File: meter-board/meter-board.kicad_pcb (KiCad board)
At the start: 2 copper layers, 0 parts

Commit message: modify pcb config
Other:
- copper layers 2 -> 4
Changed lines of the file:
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@@
 	(layers
 		(0 "F.Cu" signal)
+		(4 "In1.Cu" signal)
+		(6 "In2.Cu" signal)
 		(2 "B.Cu" signal)
 		(9 "F.Adhes" user "F.Adhesive")
@@
 		(43 "User.3" user)
 		(45 "User.4" user)
+		(47 "User.5" user)
+		(49 "User.6" user)
+		(51 "User.7" user)
+		(53 "User.8" user)
+		(55 "User.9" user)
 	)
 	(setup
@@
 			)
 			(layer "dielectric 1"
-				(type "core")
-				(thickness 0.71)
+				(type "prepreg")
+				(thickness 0.1)
 				(material "FR4")
 				(epsilon_r 4.5)
+				(loss_tangent 0.02)
+			)
+			(layer "In1.Cu"
+				(type "copper")
+				(thickness 0.035)
+			)
+			(layer "dielectric 2"
+				(type "core")
+				(thickness 0.44)
+				(material "FR4")
+				(epsilon_r 4.5)
+				(loss_tangent 0.02)
+			)
+			(layer "In2.Cu"
+				(type "copper")
+				(thickness 0.035)
+			)
+			(layer "dielectric 3"
+				(type "prepreg")
+				(thickness 0.1)
+				(material "FR4")
+				(epsilon_r 4.5)

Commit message: update layout
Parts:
- added C1: 4.7u, my_Capacitor:C_1206_3216M, B.Cu at (42.5, 44.5)
- added C10: UUD1H101MNL1GS, my_Capacitor:UUD1H101MNL1GS, B.Cu at (39.5, 37.0)
- added C11: 0.1u, my_Capacitor:C_0402_1005M, F.Cu at (4.00, 14.0)
- added C12: 0.1u, my_Capacitor:C_0402_1005M, F.Cu at (0.50, 19.5)
- added C13: 0.1u, my_Capacitor:C_0402_1005M, F.Cu at (0.50, 24.0)
- added C14: 0.1u, my_Capacitor:C_0402_1005M, F.Cu at (0.50, 28.5)
- added C15: 0.1u, my_Capacitor:C_0402_1005M, F.Cu at (33.5, 62.5)
- added C16: 0.1u, my_Capacitor:C_0402_1005M, F.Cu at (43.5, 62.5)
- added C17: 0.1u, my_Capacitor:C_0402_1005M, F.Cu at (57.0, 54.0)
- added C18: 0.1u, my_Capacitor:C_0402_1005M, F.Cu at (62.0, 54.0)
- added C19: 0.1u, ProjectEV_Capacitor:C_1005M, B.Cu at (94.5, 11.5)
- added C2: 4.7u, my_Capacitor:C_1206_3216M, B.Cu at (35.5, 45.5)
- added C20: 0.1u, ProjectEV_Capacitor:C_1005M, B.Cu at (94.5, 17.5)
- added C21: 0.1u, ProjectEV_Capacitor:C_1005M, F.Cu at (2.00, 34.5)
- added C22: 0.1u, ProjectEV_Capacitor:C_1005M, F.Cu at (113.2, 35.0)
- added C23: 1000p, my_Capacitor:C_1206_3216M, B.Cu at (12.5, 3.50)
- added C24: 10n, my_Capacitor:C_0402_1005M, F.Cu at (0.50, 26.5)
- added C25: 10n, my_Capacitor:C_0402_1005M, F.Cu at (0.50, 30.5)
- added C26: 10n, my_Capacitor:C_0402_1005M, F.Cu at (34.5, 69.0)
- added C27: 10n, my_Capacitor:C_0402_1005M, F.Cu at (45.5, 69.0)
- added C3: 10u, my_Capacitor:C_1206_3216M, F.Cu at (34.0, 45.5)
- added C4: 8p, my_Capacitor:C_0402_1005M, F.Cu at (27.5, 42.0)
- added C5: 0.1u, my_Capacitor:C_0402_1005M, F.Cu at (35.0, 43.5)
- added C6: 22u, my_Capacitor:C_1206_3216M, F.Cu at (35.0, 38.5)
- added C7: 22u, my_Capacitor:C_1206_3216M, F.Cu at (35.0, 36.0)
- added C8: 1u, my_Capacitor:C_0402_1005M, F.Cu at (31.0, 45.5)
- added C9: 6800p, my_Capacitor:C_0402_1005M, F.Cu at (27.5, 40.0)
- added D1: DF2B36FU,H3F, my_Protection:DF2B36FU,H3F, B.Cu at (52.5, 39.5)
- added D10: XZM2CRK45WT-9, my_LED:XZM2CRK45WT-9, B.Cu at (16.5, 30.5)
- added D11: XZM2CRK45WT-9, my_LED:XZM2CRK45WT-9, B.Cu at (16.5, 35.5)
- added D12: XZM2CRK45WT-9, my_LED:XZM2CRK45WT-9, B.Cu at (16.5, 40.5)
- added D13: XZM2CRK45WT-9, my_LED:XZM2CRK45WT-9, B.Cu at (16.5, 45.5)
- added D14: XZM2CRK45WT-9, my_LED:XZM2CRK45WT-9, B.Cu at (22.5, 40.5)
- added D15: XZM2CRK45WT-9, my_LED:XZM2CRK45WT-9, B.Cu at (27.5, 33.0)
- added D16: XZM2CRK45WT-9, my_LED:XZM2CRK45WT-9, B.Cu at (32.5, 28.0)
- added D17: XZM2CRK45WT-9, my_LED:XZM2CRK45WT-9, B.Cu at (37.5, 23.0)
- added D18: XZM2CRK45WT-9, my_LED:XZM2CRK45WT-9, B.Cu at (42.5, 20.5)
- added D19: XZM2CRK45WT-9, my_LED:XZM2CRK45WT-9, B.Cu at (47.5, 18.0)
- added D2: MM3Z12VST1G, my_Diode:MM3Z12VST1G, B.Cu at (45.5, 43.0)
- added D20: XZM2CRK45WT-9, my_LED:XZM2CRK45WT-9, B.Cu at (52.5, 18.0)
- added D21: XZM2CRK45WT-9, my_LED:XZM2CRK45WT-9, B.Cu at (57.5, 18.0)
- added D22: XZM2CRK45WT-9, my_LED:XZM2CRK45WT-9, B.Cu at (62.5, 18.0)
- added D23: XZM2CRK45WT-9, my_LED:XZM2CRK45WT-9, B.Cu at (67.5, 18.0)
- added D24: XZM2DG45WT-9, my_LED:XZM2DG45WT-9, B.Cu at (85.0, 25.5)
- added D25: XZM2DG45WT-9, my_LED:XZM2DG45WT-9, B.Cu at (85.0, 30.5)
- added D26: XZM2DG45WT-9, my_LED:XZM2DG45WT-9, B.Cu at (85.0, 35.5)
- added D27: XZM2DG45WT-9, my_LED:XZM2DG45WT-9, B.Cu at (85.0, 40.5)
- added D28: XZM2DG45WT-9, my_LED:XZM2DG45WT-9, B.Cu at (85.0, 45.5)
- added D29: XZM2DG45WT-9, my_LED:XZM2DG45WT-9, B.Cu at (17.5, 6.50)
- added D3: LTW-E670DS, my_LED:LTW-E670DS, F.Cu at (12.5, 13.0)
- added D30: XZM2DG45WT-9, my_LED:XZM2DG45WT-9, B.Cu at (22.5, 6.50)
- added D31: XZM2DG45WT-9, my_LED:XZM2DG45WT-9, B.Cu at (27.5, 6.50)
- added D32: XZM2DG45WT-9, my_LED:XZM2DG45WT-9, B.Cu at (32.5, 6.50)
- added D33: XZM2DG45WT-9, my_LED:XZM2DG45WT-9, B.Cu at (37.5, 6.50)
- added D34: XZM2DG45WT-9, my_LED:XZM2DG45WT-9, B.Cu at (42.5, 6.50)
- added D35: XZM2CRK45WT-9, my_LED:XZM2CRK45WT-9, B.Cu at (47.5, 6.50)
- added D36: XZM2CRK45WT-9, my_LED:XZM2CRK45WT-9, B.Cu at (52.5, 6.50)
- added D37: XZM2CRK45WT-9, my_LED:XZM2CRK45WT-9, B.Cu at (57.5, 6.50)
- added D38: XZM2CRK45WT-9, my_LED:XZM2CRK45WT-9, B.Cu at (62.5, 6.50)
- added D39: XZM2CRK45WT-9, my_LED:XZM2CRK45WT-9, B.Cu at (67.5, 6.50)
- added D4: LTW-E670DS, my_LED:LTW-E670DS, F.Cu at (17.5, 13.0)
- added D40: XZM2CRK45WT-9, my_LED:XZM2CRK45WT-9, B.Cu at (72.5, 6.50)
- added D41: BAS70-04-E3-08, my_Diode:BAS70-04-E3-08, B.Cu at (31.0, 99.0)
- added D42: BAS70-04-E3-08, my_Diode:BAS70-04-E3-08, B.Cu at (31.0, 103.5)
- added D43: BAS70-04-E3-08, my_Diode:BAS70-04-E3-08, B.Cu at (29.9, 87.5)
- added D44: BAS70-04-E3-08, my_Diode:BAS70-04-E3-08, B.Cu at (33.5, 87.5)
- added D45: BAS70-04-E3-08, my_Diode:BAS70-04-E3-08, B.Cu at (26.4, 99.0)
- added D46: BAS70-04-E3-08, my_Diode:BAS70-04-E3-08, B.Cu at (26.4, 103.5)
- added D47: BAS70-04-E3-08, my_Diode:BAS70-04-E3-08, B.Cu at (26.4, 107.9)
- added D48: DF2B36FU,H3F, my_Protection:DF2B36FU,H3F, B.Cu at (70.5, 104.0)
- added D49: DF2B36FU,H3F, my_Protection:DF2B36FU,H3F, B.Cu at (40.0, 92.5)
- added D5: LTW-E670DS, my_LED:LTW-E670DS, F.Cu at (22.5, 13.0)
- added D50: DF2B36FU,H3F, my_Protection:DF2B36FU,H3F, B.Cu at (29.9, 94.5)
- added D51: DF2B36FU,H3F, my_Protection:DF2B36FU,H3F, B.Cu at (45.0, 100.0)
- added D52: DF2B36FU,H3F, my_Protection:DF2B36FU,H3F, B.Cu at (40.0, 104.5)
- added D53: DF2B36FU,H3F, my_Protection:DF2B36FU,H3F, B.Cu at (40.5, 109.0)
- added D54: DF2B36FU,H3F, my_Protection:DF2B36FU,H3F, B.Cu at (53.0, 99.5)
- added D55: 150060GS75003, my_LED:150060GS75003, F.Cu at (26.5, 44.0)
- added D6: LTW-E670DS, my_LED:LTW-E670DS, F.Cu at (27.5, 13.0)
- added D7: XZM2CRK45WT, my_LED:XZM2CRK45WT, F.Cu at (80.0, 6.50)
- added D8: XZMECBDDG45SHTA, my_LED:XZMECBDDG45SHTA, F.Cu at (32.5, 13.0)
- added D9: XZM2CRK45WT-9, my_LED:XZM2CRK45WT-9, B.Cu at (16.5, 25.5)
- added F1: 0686F0500-01, my_Fuse:0686F0500-01, B.Cu at (49.5, 40.0)
- added FB1: MMZ1005Y102CT000, my_Filter:MMZ1005Y102CT000, B.Cu at (42.0, 31.5)
- added FL1: ACP3225-102-2P-T000, my_Filter:ACP3225-102-2P-T000, B.Cu at (39.0, 44.5)
- added H1: MountingHole_4.3mm_M4_Pad_Via, my_Mechanical:MountingHole_4.3mm_M4_Pad_Via, F.Cu at (5.00, 5.00)
- added H2: MountingHole_4.3mm_M4_Pad_Via, my_Mechanical:MountingHole_4.3mm_M4_Pad_Via, F.Cu at (5.00, 45.0)
- added H3: MountingHole_4.3mm_M4_Pad_Via, my_Mechanical:MountingHole_4.3mm_M4_Pad_Via, F.Cu at (95.0, 45.0)
- added H4: MountingHole_4.3mm_M4_Pad_Via, my_Mechanical:MountingHole_4.3mm_M4_Pad_Via, F.Cu at (95.0, 5.00)
- added J1: 2-1445053-2, my_Connector:2-1445053-2, B.Cu at (51.0, 46.5)
- added J2: 3-794636-8, my_Connector:3-794636-8, B.Cu at (68.5, 34.0)
- added J3: 2-1445053-4, my_Connector:2-1445053-4, B.Cu at (68.5, 46.5)
- added JP1: SolderJumper-2_P1.3mm_Open_RoundedPad1.0x1.5mm, my_Jumper:SolderJumper-2_P1.3mm_Open_RoundedPad1.0x1.5mm, F.Cu at (24.5, 46.5)
- added JP2: SolderJumper-2_P1.3mm_Open_RoundedPad1.0x1.5mm, my_Jumper:SolderJumper-2_P1.3mm_Open_RoundedPad1.0x1.5mm, F.Cu at (27.0, 46.5)
- added L1: SRP2512TMA-2R2M, my_Inductor:SRP2512TMA-2R2M, F.Cu at (36.5, 41.5)
- added Q1: PMN100EPAX, my_Transistor:PMN100EPAX, B.Cu at (46.5, 40.0)
- added Q2: 2N7002K-AU_R1_000A2, my_Transistor:2N7002K-AU_R1_000A2, B.Cu at (26.0, 46.0)
- added R1: 10k, my_Resistor:R_0402_1005M, B.Cu at (48.0, 43.0)
- added R10: 2.2k, my_Resistor:R_0402_1005M, B.Cu at (20.0, 3.50)
- added R100: 100k, my_Resistor:R_0402_1005M, F.Cu at (94.0, 28.0)
- added R101: 100k, my_Resistor:R_0402_1005M, F.Cu at (94.0, 29.0)
- added R102: 100k, my_Resistor:R_0402_1005M, F.Cu at (94.0, 30.0)
- added R103: 100k, my_Resistor:R_0402_1005M, F.Cu at (94.0, 31.0)
- added R104: 100k, my_Resistor:R_0402_1005M, F.Cu at (94.0, 32.0)
- added R105: 100k, my_Resistor:R_0402_1005M, F.Cu at (94.0, 33.0)
- added R106: 100k, my_Resistor:R_0402_1005M, B.Cu at (24.5, 18.0)
- added R107: 100k, my_Resistor:R_0402_1005M, B.Cu at (24.5, 19.0)
- added R108: 100k, my_Resistor:R_0402_1005M, B.Cu at (24.5, 20.0)
- added R109: 100k, my_Resistor:R_0402_1005M, B.Cu at (24.5, 21.0)
- added R11: 2.2k, my_Resistor:R_0402_1005M, B.Cu at (25.0, 3.50)
- added R110: 100k, my_Resistor:R_0402_1005M, B.Cu at (24.5, 22.0)
- added R111: 100k, my_Resistor:R_0402_1005M, B.Cu at (24.5, 23.0)
- added R112: 100k, my_Resistor:R_0402_1005M, B.Cu at (24.5, 24.0)
- added R113: 100k, my_Resistor:R_0402_1005M, B.Cu at (24.5, 25.0)
- added R114: ST-4ETA103, my_Resistor:ST-4ETA103, B.Cu at (20.0, 65.0)
- added R115: ST-4ETA103, my_Resistor:ST-4ETA103, B.Cu at (27.0, 65.0)
- added R116: ST-4ETA103, my_Resistor:ST-4ETA103, B.Cu at (56.0, 63.5)
- added R117: ST-4ETA103, my_Resistor:ST-4ETA103, B.Cu at (62.0, 63.5)
- added R118: 220, my_Resistor:R_0603_1608M, B.Cu at (77.5, 5.00)
- added R119: 220, my_Resistor:R_0603_1608M, B.Cu at (77.5, 6.50)
- added R12: 2.2k, my_Resistor:R_0402_1005M, B.Cu at (30.0, 3.50)
- added R120: 220, my_Resistor:R_0603_1608M, B.Cu at (77.5, 8.00)
- added R121: 220, my_Resistor:R_0603_1608M, B.Cu at (77.5, 9.50)
- added R122: 220, my_Resistor:R_0603_1608M, B.Cu at (77.5, 11.0)
- added R123: 220, my_Resistor:R_0603_1608M, B.Cu at (77.5, 12.5)
- added R124: 220, my_Resistor:R_0603_1608M, B.Cu at (77.5, 14.0)
- added R125: 220, my_Resistor:R_0603_1608M, B.Cu at (77.5, 15.5)
- added R126: 100k, my_Resistor:R_0402_1005M, B.Cu at (89.0, 7.00)
- added R127: 100k, my_Resistor:R_0402_1005M, B.Cu at (89.0, 8.00)
- added R128: 100k, my_Resistor:R_0402_1005M, B.Cu at (89.0, 9.00)
- added R129: 100k, my_Resistor:R_0402_1005M, B.Cu at (89.0, 10.0)
- added R13: 2.2k, my_Resistor:R_0402_1005M, B.Cu at (35.0, 3.50)
- added R130: 100k, my_Resistor:R_0402_1005M, B.Cu at (89.0, 11.0)
- added R131: 100k, my_Resistor:R_0402_1005M, B.Cu at (89.0, 12.0)
- added R132: 100k, my_Resistor:R_0402_1005M, B.Cu at (89.0, 13.0)
- added R133: 100k, my_Resistor:R_0402_1005M, B.Cu at (89.0, 14.0)
- added R134: 100k, my_Resistor:R_0402_1005M, B.Cu at (89.0, 15.0)
- added R135: 100k, my_Resistor:R_0402_1005M, B.Cu at (89.0, 16.0)
- added R136: 100k, my_Resistor:R_0402_1005M, B.Cu at (89.0, 17.0)
- added R137: 100k, my_Resistor:R_0402_1005M, B.Cu at (89.0, 18.0)
- added R138: 100k, my_Resistor:R_0402_1005M, B.Cu at (89.0, 19.0)
- added R139: 100k, my_Resistor:R_0402_1005M, B.Cu at (89.0, 20.0)
- added R14: 2.2k, my_Resistor:R_0402_1005M, B.Cu at (40.0, 3.50)
- added R140: 100k, my_Resistor:R_0402_1005M, B.Cu at (89.0, 21.0)
- added R141: 100k, my_Resistor:R_0402_1005M, B.Cu at (89.0, 22.0)
- added R142: 100k, my_Resistor:R_0402_1005M, B.Cu at (10.5, 33.0)
- added R143: 100k, my_Resistor:R_0402_1005M, B.Cu at (10.5, 34.0)
- added R144: 100k, my_Resistor:R_0402_1005M, B.Cu at (10.5, 35.0)
- added R145: 100k, my_Resistor:R_0402_1005M, B.Cu at (10.5, 36.0)
- added R146: 100k, my_Resistor:R_0402_1005M, B.Cu at (10.5, 37.0)
- added R147: 100k, my_Resistor:R_0402_1005M, B.Cu at (10.5, 38.0)
- added R148: 100k, my_Resistor:R_0402_1005M, B.Cu at (10.5, 39.0)
- added R149: 100k, my_Resistor:R_0402_1005M, B.Cu at (10.5, 40.0)
- added R15: 2.2k, my_Resistor:R_0402_1005M, B.Cu at (45.0, 3.50)
- added R150: 100k, my_Resistor:R_0402_1005M, F.Cu at (111.2, 28.1)
- added R151: 100k, my_Resistor:R_0402_1005M, F.Cu at (111.2, 30.1)
- added R152: 100k, my_Resistor:R_0402_1005M, F.Cu at (111.2, 32.0)
- added R153: 100k, my_Resistor:R_0402_1005M, F.Cu at (-1.50, 26.5)
- added R154: 100k, my_Resistor:R_0402_1005M, F.Cu at (0.50, 31.5)
- added R155: 100k, my_Resistor:R_0402_1005M, F.Cu at (34.5, 68.0)
- added R156: 100k, my_Resistor:R_0402_1005M, F.Cu at (45.5, 68.0)
- added R157: 100, my_Resistor:R_0402_1005M, B.Cu at (23.9, 91.5)
- added R158: 100, my_Resistor:R_0402_1005M, B.Cu at (39.0, 113.5)
- added R159: 100, my_Resistor:R_0402_1005M, B.Cu at (29.9, 91.5)
- added R16: 2.2k, my_Resistor:R_0402_1005M, B.Cu at (50.0, 3.50)
- added R160: 100, my_Resistor:R_0402_1005M, B.Cu at (36.0, 97.9)
- added R161: 100, my_Resistor:R_0402_1005M, B.Cu at (36.0, 99.8)
- added R162: 100, my_Resistor:R_0402_1005M, B.Cu at (36.0, 101.8)
- added R163: 100, my_Resistor:R_0402_1005M, B.Cu at (36.0, 103.8)
- added R164: 1M, my_Resistor:R_1206_3216M, B.Cu at (12.5, 6.50)
- added R165: 100k, my_Resistor:R_0402_1005M, F.Cu at (24.5, 44.0)
- added R166: 100k, my_Resistor:R_0402_1005M, B.Cu at (28.5, 45.0)
- added R167: 100, my_Resistor:R_0402_1005M, B.Cu at (28.5, 43.0)
- added R17: 2.2k, my_Resistor:R_0402_1005M, B.Cu at (55.0, 3.50)
- added R18: 2.2k, my_Resistor:R_0402_1005M, B.Cu at (60.0, 3.50)
- added R19: 2.2k, my_Resistor:R_0402_1005M, B.Cu at (65.0, 3.50)
- added R2: 100k, my_Resistor:R_0402_1005M, F.Cu at (30.0, 37.0)
- added R20: 2.2k, my_Resistor:R_0402_1005M, B.Cu at (70.0, 3.50)
- added R21: 2.2k, my_Resistor:R_0402_1005M, B.Cu at (75.0, 3.50)
- added R22: 2.2k, my_Resistor:R_0402_1005M, F.Cu at (15.0, 15.0)
- added R23: 2.2k, my_Resistor:R_0402_1005M, F.Cu at (20.0, 15.0)
- added R24: 2.2k, my_Resistor:R_0402_1005M, F.Cu at (25.0, 15.0)
- added R25: 2.2k, my_Resistor:R_0402_1005M, F.Cu at (30.0, 15.0)
- added R26: 2.2k, my_Resistor:R_0402_1005M, F.Cu at (34.5, 17.0)
- added R27: 2.2k, my_Resistor:R_0402_1005M, F.Cu at (32.5, 17.0)
- added R28: 2.2k, my_Resistor:R_0402_1005M, F.Cu at (33.5, 17.0)
- added R29: 2.2k, my_Resistor:R_0402_1005M, B.Cu at (13.5, 23.0)
- added R3: 18k, my_Resistor:R_0402_1005M, F.Cu at (30.0, 38.0)
- added R30: 2.2k, my_Resistor:R_0402_1005M, B.Cu at (13.5, 28.0)
- added R31: 2.2k, my_Resistor:R_0402_1005M, B.Cu at (13.5, 33.0)
- added R32: 2.2k, my_Resistor:R_0402_1005M, B.Cu at (13.5, 38.0)
- added R33: 2.2k, my_Resistor:R_0402_1005M, B.Cu at (13.5, 43.0)
- added R34: 2.2k, my_Resistor:R_0402_1005M, B.Cu at (22.5, 35.5)
- added R35: 2.2k, my_Resistor:R_0402_1005M, B.Cu at (27.5, 28.0)
- added R36: 2.2k, my_Resistor:R_0402_1005M, B.Cu at (32.5, 23.0)
- added R37: 2.2k, my_Resistor:R_0402_1005M, B.Cu at (37.5, 18.0)
- added R38: 2.2k, my_Resistor:R_0402_1005M, B.Cu at (42.5, 15.5)
- added R39: 2.2k, my_Resistor:R_0402_1005M, B.Cu at (47.5, 13.0)
- added R4: 100k, my_Resistor:R_0402_1005M, F.Cu at (26.5, 42.0)
- added R40: 2.2k, my_Resistor:R_0402_1005M, B.Cu at (52.5, 13.0)
- added R41: 2.2k, my_Resistor:R_0402_1005M, B.Cu at (57.5, 13.0)
- added R42: 2.2k, my_Resistor:R_0402_1005M, B.Cu at (62.5, 13.0)
- added R43: 2.2k, my_Resistor:R_0402_1005M, B.Cu at (67.5, 13.0)
- added R44: 2.2k, my_Resistor:R_0402_1005M, F.Cu at (78.5, 4.00)
- added R45: 2.2k, my_Resistor:R_0402_1005M, B.Cu at (82.0, 23.0)
- added R46: 2.2k, my_Resistor:R_0402_1005M, B.Cu at (82.0, 28.0)
- added R47: 2.2k, my_Resistor:R_0402_1005M, B.Cu at (82.0, 33.0)
- added R48: 2.2k, my_Resistor:R_0402_1005M, B.Cu at (82.0, 38.0)
- added R49: 2.2k, my_Resistor:R_0402_1005M, B.Cu at (82.0, 43.0)
- added R5: 19.1k, my_Resistor:R_0402_1005M, F.Cu at (28.5, 43.0)
- added R50: 2.2k, my_Resistor:R_0402_1005M, B.Cu at (7.50, 15.0)
- added R51: 2.2k, my_Resistor:R_0402_1005M, B.Cu at (7.50, 16.0)
- added R52: 2.2k, my_Resistor:R_0402_1005M, B.Cu at (7.50, 17.0)
- added R53: 2.2k, my_Resistor:R_0402_1005M, B.Cu at (7.50, 18.0)
- added R54: 2.2k, my_Resistor:R_0402_1005M, B.Cu at (7.50, 19.0)
- added R55: 2.2k, my_Resistor:R_0402_1005M, B.Cu at (7.50, 20.0)
- added R56: 2.2k, my_Resistor:R_0402_1005M, B.Cu at (7.50, 21.0)
- added R57: 2.2k, my_Resistor:R_0402_1005M, B.Cu at (7.50, 22.0)
- added R58: 2.2k, my_Resistor:R_0402_1005M, B.Cu at (7.50, 23.0)
- added R59: 2.2k, my_Resistor:R_0402_1005M, B.Cu at (7.50, 24.0)
- added R6: 82k, my_Resistor:R_0402_1005M, F.Cu at (30.0, 39.0)
- added R60: 2.2k, my_Resistor:R_0402_1005M, B.Cu at (7.50, 25.0)
- added R61: 2.2k, my_Resistor:R_0402_1005M, B.Cu at (7.50, 26.0)
- added R62: 2.2k, my_Resistor:R_0402_1005M, B.Cu at (7.50, 27.0)
- added R63: 2.2k, my_Resistor:R_0402_1005M, F.Cu at (16.0, 65.0)
- added R64: 2.2k, my_Resistor:R_0402_1005M, F.Cu at (16.0, 66.0)
- added R65: 2.2k, my_Resistor:R_0402_1005M, F.Cu at (16.0, 67.0)
- added R66: 2.2k, my_Resistor:R_0402_1005M, F.Cu at (16.0, 68.0)
- added R67: 2.2k, my_Resistor:R_0402_1005M, F.Cu at (38.0, 62.0)
- added R68: 2.2k, my_Resistor:R_0402_1005M, F.Cu at (38.0, 63.0)
- added R69: 2.2k, my_Resistor:R_0402_1005M, F.Cu at (38.0, 64.0)
- added R7: 9.1k, my_Resistor:R_0402_1005M, B.Cu at (32.0, 39.0)
- added R70: 2.2k, my_Resistor:R_0402_1005M, F.Cu at (38.0, 65.0)
- added R71: 2.2k, my_Resistor:R_0402_1005M, F.Cu at (38.0, 66.0)
- added R72: 2.2k, my_Resistor:R_0402_1005M, F.Cu at (38.0, 67.0)
- added R73: 1k, my_Resistor:R_0402_1005M, F.Cu at (52.0, 65.0)
- added R74: 1k, my_Resistor:R_0402_1005M, F.Cu at (52.0, 57.0)
- added R75: 1k, my_Resistor:R_0402_1005M, F.Cu at (52.0, 58.0)
- added R76: 1k, my_Resistor:R_0402_1005M, F.Cu at (52.0, 59.0)
- added R77: 1k, my_Resistor:R_0402_1005M, F.Cu at (52.0, 60.0)
- added R78: 1k, my_Resistor:R_0402_1005M, F.Cu at (52.0, 61.0)
- added R79: 1k, my_Resistor:R_0402_1005M, F.Cu at (52.0, 62.0)
- added R8: 3k, my_Resistor:R_0402_1005M, B.Cu at (30.0, 39.0)
- added R80: 1k, my_Resistor:R_0402_1005M, F.Cu at (52.0, 63.0)
- added R81: 1k, my_Resistor:R_0402_1005M, F.Cu at (52.0, 64.0)
- added R82: 100k, my_Resistor:R_0402_1005M, B.Cu at (10.5, 15.0)
- added R83: 100k, my_Resistor:R_0402_1005M, B.Cu at (10.5, 16.0)
- added R84: 100k, my_Resistor:R_0402_1005M, B.Cu at (10.5, 17.0)
- added R85: 100k, my_Resistor:R_0402_1005M, B.Cu at (10.5, 18.0)
- added R86: 100k, my_Resistor:R_0402_1005M, B.Cu at (10.5, 19.0)
- added R87: 100k, my_Resistor:R_0402_1005M, B.Cu at (10.5, 20.0)
- added R88: 100k, my_Resistor:R_0402_1005M, B.Cu at (10.5, 21.0)
- added R89: 100k, my_Resistor:R_0402_1005M, B.Cu at (10.5, 22.0)
- added R9: 1k, my_Resistor:R_1206_3216M, B.Cu at (34.0, 40.5)
- added R90: 100k, my_Resistor:R_0402_1005M, B.Cu at (10.5, 24.0)
- added R91: 100k, my_Resistor:R_0402_1005M, B.Cu at (10.5, 25.0)
- added R92: 100k, my_Resistor:R_0402_1005M, B.Cu at (10.5, 26.0)
- added R93: 100k, my_Resistor:R_0402_1005M, B.Cu at (10.5, 27.0)
- added R94: 100k, my_Resistor:R_0402_1005M, B.Cu at (10.5, 28.0)
- added R95: 100k, my_Resistor:R_0402_1005M, B.Cu at (10.5, 29.0)
- added R96: 100k, my_Resistor:R_0402_1005M, B.Cu at (10.5, 30.0)
- added R97: 100k, my_Resistor:R_0402_1005M, B.Cu at (10.5, 31.0)
- added R98: 100k, my_Resistor:R_0402_1005M, F.Cu at (94.0, 26.0)
- added R99: 100k, my_Resistor:R_0402_1005M, F.Cu at (94.0, 27.0)
- added U1: AP66300QFVBW-13, my_Regulator:AP66300QFVBW-13, F.Cu at (31.5, 42.0)
- added U10: TLV1814RTER, my_Comparator:TLV1814RTER, F.Cu at (3.50, 21.0)
- added U11: TLV1814RTER, my_Comparator:TLV1814RTER, F.Cu at (3.50, 25.5)
- added U12: TLV1814RTER, my_Comparator:TLV1814RTER, F.Cu at (3.50, 30.0)
- added U13: TLV1814RTER, my_Comparator:TLV1814RTER, F.Cu at (34.0, 65.0)
- added U14: TLV1814RTER, my_Comparator:TLV1814RTER, F.Cu at (44.5, 65.0)
- added U15: TLV1814RTER, my_Comparator:TLV1814RTER, F.Cu at (57.5, 56.5)
- added U16: TBD62183AFNG,EL, my_PMIC:TBD62183AFNG,EL, F.Cu at (10.0, 19.0)
- added U17: TBD62183AFNG,EL, my_PMIC:TBD62183AFNG,EL, F.Cu at (10.0, 28.0)
- added U18: TBD62183AFNG,EL, my_PMIC:TBD62183AFNG,EL, B.Cu at (94.0, 30.0)
- added U19: TBD62183AFNG,EL, my_PMIC:TBD62183AFNG,EL, F.Cu at (24.5, 22.0)
- added U2: TS431BIYLT, my_Reference:TS431BIYLT, B.Cu at (32.5, 36.5)
- added U20: TLV1814RTER, my_Comparator:TLV1814RTER, F.Cu at (63.0, 56.5)
- added U21: SN74HC595BRWNR, my_Logic:SN74HC595BRWNR, B.Cu at (94.5, 14.0)
- added U22: SN74HC595BRWNR, my_Logic:SN74HC595BRWNR, B.Cu at (94.5, 20.0)
- added U23: SN74HC595BRWNR, my_Logic:SN74HC595BRWNR, F.Cu at (3.50, 37.0)
- added U24: TBD62783AFNG,EL, my_PMIC:TBD62783AFNG,EL, B.Cu at (83.5, 11.0)
- added U25: TBD62183AFNG,EL, my_PMIC:TBD62183AFNG,EL, B.Cu at (83.5, 19.0)
- added U26: TBD62183AFNG,EL, my_PMIC:TBD62183AFNG,EL, F.Cu at (10.0, 37.0)
- added U27: SN74LV4T125RGYR, my_Logic:SN74LV4T125RGYR, F.Cu at (111.3, 38.0)
- added U3: ACSC02-41SURKWA-F01, my_LED:ACSC02-41SURKWA-F01, F.Cu at (75.0, 16.5)
- added U4: ACSC02-41SURKWA-F01, my_LED:ACSC02-41SURKWA-F01, F.Cu at (82.5, 16.5)
- added U5: ACSC02-41SURKWA-F01, my_LED:ACSC02-41SURKWA-F01, F.Cu at (90.0, 16.5)
- added U6: 157121S12700, my_LED:157121S12700, F.Cu at (44.0, 38.5)
- added U7: 157121S12700, my_LED:157121S12700, F.Cu at (54.5, 38.5)
- added U8: 157121S12700, my_LED:157121S12700, F.Cu at (65.0, 38.5)
- added U9: TLV1814RTER, my_Comparator:TLV1814RTER, F.Cu at (3.50, 16.5)
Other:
- board outline added: 100 x 50 mm
- board text added: "V"
- board text added: "km/h"

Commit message: update layout
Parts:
- C19, C20, U18, U21, U22: moved to F.Cu
- C24, R100, R101, R102, R103, R104, R105, R153, R63, R64, R65, R66, R98, R99: moved to B.Cu
- moved D47 84.9 mm to (78.0, 40.5), turned to -90 degrees
- moved R158 77.7 mm to (64.0, 40.0)
- moved D46 77.6 mm to (74.5, 42.5), turned to -90 degrees
- moved D53 77.3 mm to (74.5, 39.5), turned to 0 degrees
- moved D45 73.6 mm to (78.0, 46.5), turned to -90 degrees
- moved D52 71.9 mm to (78.0, 43.5), turned to 0 degrees
- moved R163 71.4 mm to (71.0, 41.5), turned to 0 degrees
- moved R162 68.2 mm to (68.0, 41.5), turned to 0 degrees
- moved D51 67.6 mm to (54.0, 33.0)
- moved R160 67.1 mm to (70.0, 40.0)
- moved D54 66.8 mm to (78.0, 37.5), turned to 0 degrees
- moved D42 65.6 mm to (54.0, 42.0), turned to 90 degrees
- moved D50 65.5 mm to (57.5, 35.0), turned to 180 degrees
- moved R161 65.1 mm to (65.0, 41.5), turned to 0 degrees
- moved D48 64.3 mm to (57.5, 41.0), turned to 180 degrees
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
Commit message: layout of components is finished
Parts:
- moved D14 0.50 mm to (22.5, 41.0)
- moved Q2 0.50 mm to (26.5, 46.0)
- moved R166 0.50 mm to (29.0, 45.0)
- moved R167 0.50 mm to (29.0, 43.0)

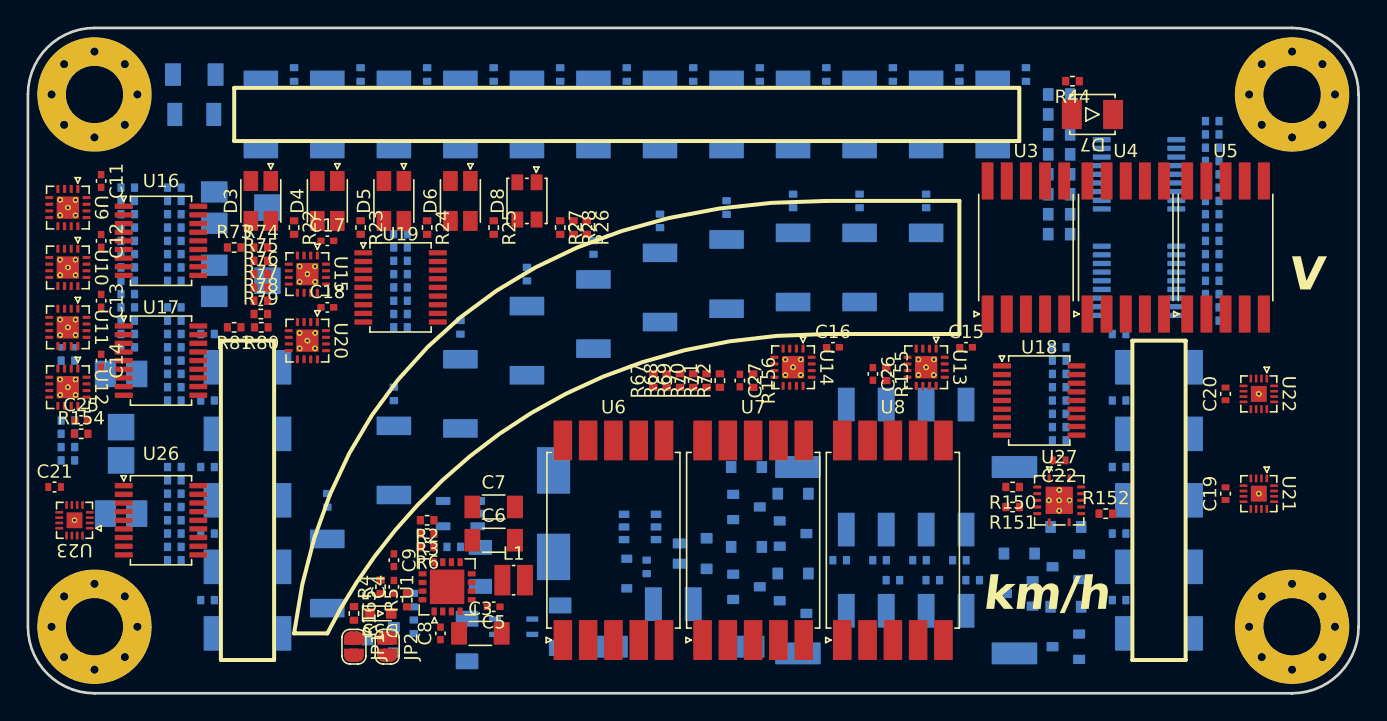
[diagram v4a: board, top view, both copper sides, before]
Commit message: update wiring
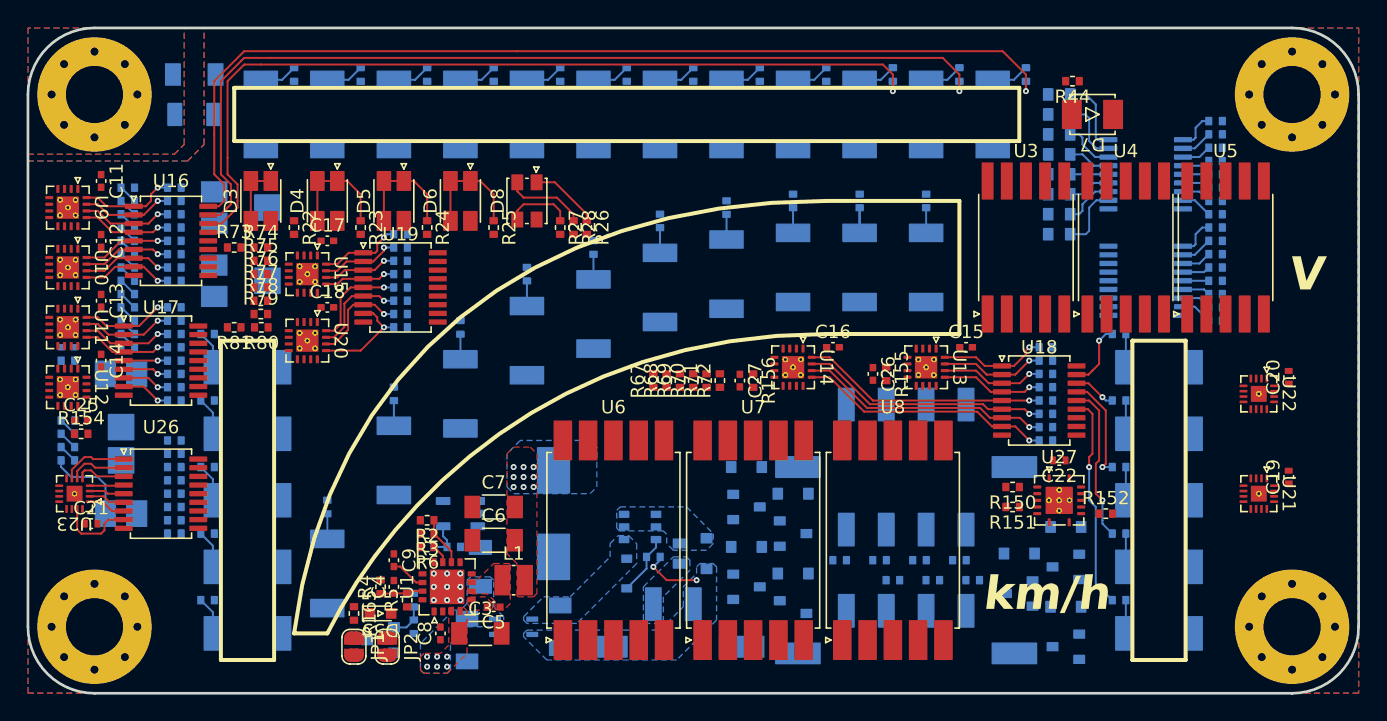
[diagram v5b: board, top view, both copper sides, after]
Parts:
- moved C19 4.91 mm to (94.8, 33.8)
- moved C20 4.91 mm to (94.8, 26.2)
- moved C21 3.89 mm to (4.75, 37.2)
- moved R142 2.00 mm to (11.0, 31.0)
- moved R143 2.00 mm to (11.0, 32.0)
- moved R144 2.00 mm to (11.0, 33.0)
- moved R145 2.00 mm to (11.0, 34.0)
- moved R146 2.00 mm to (11.0, 35.0)
- moved R147 2.00 mm to (11.0, 36.0)
- moved R148 2.00 mm to (11.0, 37.0)
- moved R149 2.00 mm to (11.0, 38.0)
- moved U23 2.00 mm to (3.50, 35.0)
- moved U26 2.00 mm to (10.0, 35.0)
- moved R100 1.00 mm to (76.5, 26.0)
- moved R101 1.00 mm to (76.5, 27.0)
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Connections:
- D8 pad 2: (no net) -> +5VD
- J1 pad MP1: GND -> Net-(D1-A2)
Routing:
- net /G6R6_R6: track 0.00 -> 75.3 mm, vias 0 -> 1
- net /G6R6_R5: track 0.00 -> 70.3 mm, vias 0 -> 1
- net /G6R6_R4: track 0.00 -> 65.3 mm, vias 0 -> 1
- net Net-(U18-I8): track 0.00 -> 19.1 mm, vias 0 -> 1
- net Net-(U18-I7): track 0.00 -> 18.9 mm, vias 0 -> 1
- net Net-(U18-I6): track 0.00 -> 18.6 mm, vias 0 -> 1
- net Net-(U18-I5): track 0.00 -> 18.4 mm, vias 0 -> 1
- net /G5_G1: track 0.00 -> 16.2 mm, vias 0 -> 1
- net /G5_G2: track 0.00 -> 11.9 mm, vias 0 -> 1
- net Net-(D6-K-Pad1): track 0.00 -> 8.65 mm
- net Net-(D4-K-Pad1): track 0.00 -> 8.65 mm
- net Net-(D5-K-Pad1): track 0.00 -> 8.65 mm
- net Net-(U18-I1): track 0.00 -> 8.09 mm, vias 0 -> 1
- net Net-(U19-I8): track 0.00 -> 7.95 mm, vias 0 -> 1
- net /G5_G3: track 0.00 -> 7.87 mm, vias 0 -> 1
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- added copper zone on B.Cu, net +5VD
- added copper zone on F.Cu, net +5VD
- added copper zone on B.Cu, net /VIN
- added copper zone on F.Cu, net /VIN
- added copper zone on B.Cu, net Chassis
- added copper zone on F.Cu, net Chassis
- added copper zone on In1.Cu, net Chassis
- added copper zone on In2.Cu, net Chassis
- added copper zone on B.Cu, net GND
- added copper zone on F.Cu, net GND
- added copper zone on In1.Cu, net GND
- added copper zone on In2.Cu, net GND
- added copper zone on F.Cu, net Net-(C5-Pad1)
- added copper zone on B.Cu, net Net-(D1-A1)
- added copper zone on B.Cu, net Net-(D1-A2)
- added copper zone on B.Cu, net Net-(D2-K)
- added copper zone on B.Cu, net Net-(J1-Pin_1)
- added copper zone on F.Cu, net Net-(U1-BST)

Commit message: update AW
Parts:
- moved R133 13.4 mm to (81.0, 3.50), turned to 90 degrees
- moved R132 12.0 mm to (82.0, 3.50), turned to 90 degrees
- moved R141 11.3 mm to (81.0, 14.2), turned to 90 degrees
- moved R131 10.6 mm to (83.0, 3.50), turned to 90 degrees
- moved R140 9.91 mm to (82.0, 14.2), turned to 90 degrees
- moved R130 9.15 mm to (84.0, 3.50), turned to 90 degrees
- moved R139 8.49 mm to (83.0, 14.2), turned to 90 degrees
- moved R129 7.77 mm to (85.0, 3.50), turned to 90 degrees
- moved R138 7.08 mm to (84.0, 14.2), turned to 90 degrees
- moved R128 6.39 mm to (86.0, 3.50), turned to 90 degrees
- moved R137 5.67 mm to (85.0, 14.2), turned to 90 degrees
- moved R127 5.03 mm to (87.0, 3.50), turned to 90 degrees
- moved R136 4.26 mm to (86.0, 14.2), turned to 90 degrees
- moved R126 3.72 mm to (88.0, 3.50), turned to 90 degrees
- moved R135 2.85 mm to (87.0, 14.2), turned to 90 degrees
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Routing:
- net +5VD: track 0.00 -> 186.7 mm, vias 9 -> 13
- net /G6R6_R3: track 0.00 -> 60.1 mm, vias 0 -> 1
- net /G6R6_R2: track 0.00 -> 55.0 mm, vias 0 -> 1
- net Net-(U21-QA): track 2.37 -> 49.3 mm, vias 0 -> 1
- net Net-(U21-QB): track 2.23 -> 46.5 mm, vias 0 -> 1
- net Net-(U21-QC): track 2.08 -> 45.6 mm, vias 0 -> 1
- net Net-(U21-QD): track 1.94 -> 44.6 mm, vias 0 -> 1
- net Net-(U21-QF): track 2.23 -> 44.8 mm, vias 0 -> 1
- net Net-(U21-QG): track 2.37 -> 44.8 mm, vias 0 -> 1
- net Net-(U21-QH): track 2.96 -> 44.8 mm, vias 0 -> 1
- net Net-(U21-QE): track 2.08 -> 43.9 mm, vias 0 -> 1
- net Net-(U22-QA): track 2.37 -> 34.1 mm, vias 0 -> 1
- net Net-(U22-QB): track 2.23 -> 30.6 mm, vias 0 -> 1
- net Net-(U22-QC): track 2.08 -> 29.5 mm, vias 0 -> 1
- net Net-(U22-QD): track 1.94 -> 28.5 mm, vias 0 -> 1
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- added copper zone on B.Cu, net +5VREF

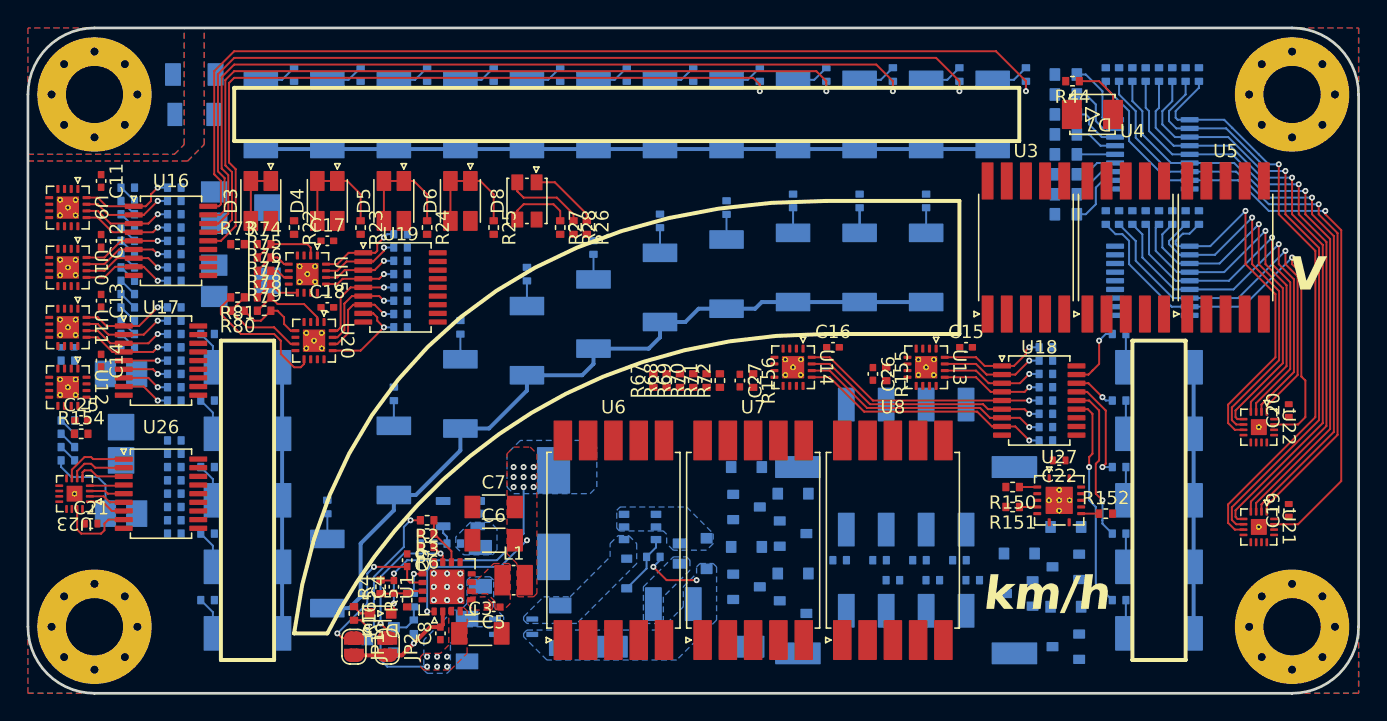
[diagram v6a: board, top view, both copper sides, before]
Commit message: update patterns
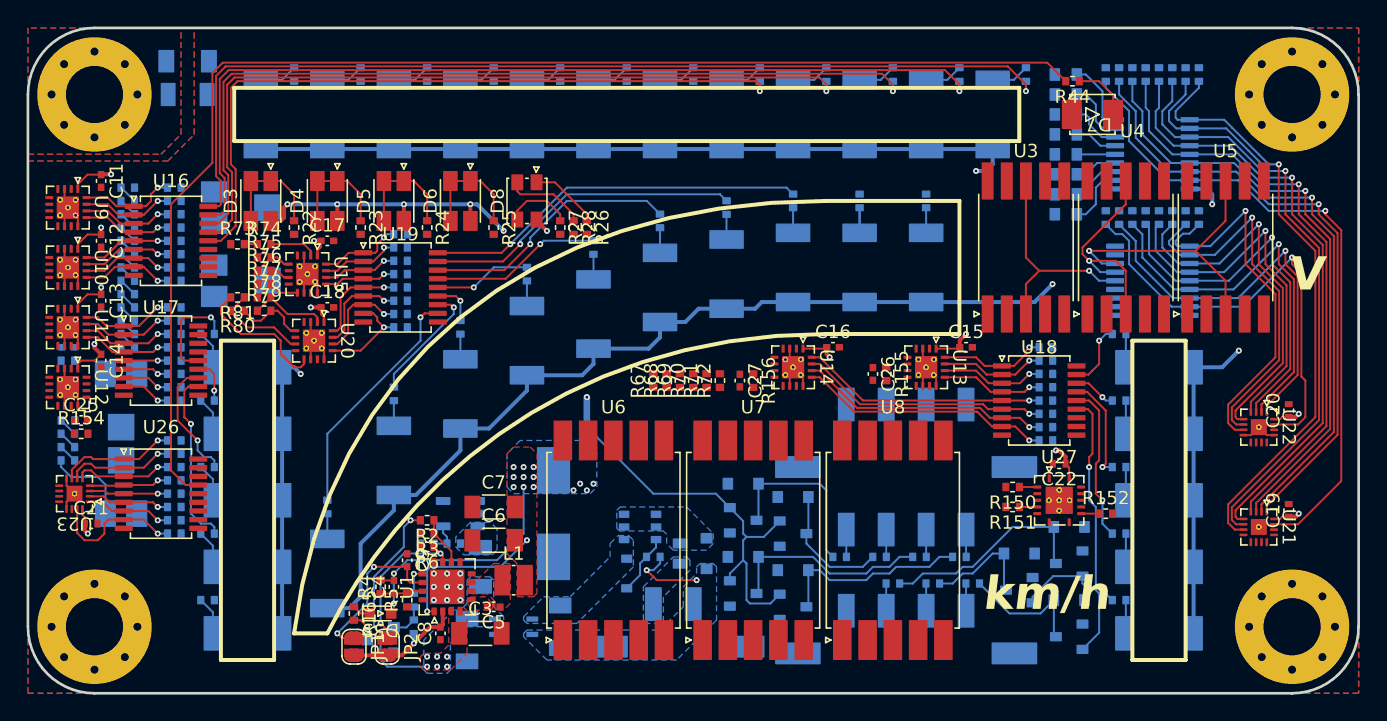
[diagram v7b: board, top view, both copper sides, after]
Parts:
- moved D51 8.50 mm to (57.5, 40.8)
- moved D44 8.28 mm to (57.5, 43.5)
- moved D41 7.94 mm to (53.8, 37.0)
- moved D48 7.72 mm to (53.8, 34.2)
- moved D45 6.25 mm to (78.2, 40.2)
- moved D50 6.05 mm to (53.8, 39.8)
- moved D52 6.01 mm to (78.2, 37.5)
- moved D43 5.86 mm to (53.8, 42.5)
- moved D54 5.51 mm to (78.2, 43.0)
- moved D42 5.32 mm to (57.5, 38.0)
- moved D47 5.26 mm to (78.2, 45.8)
- moved D49 5.13 mm to (57.5, 35.2)
- moved R164 1.58 mm to (12.0, 5.00)
- moved C23 1.12 mm to (12.0, 2.50)
- moved C22 0.25 mm to (77.5, 32.8)
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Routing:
- net +5VA: track 0.00 -> 180.1 mm, vias 0 -> 9
- net +5VD: track 186.7 -> 307.2 mm, vias 13 -> 32
- net /R1_R1: track 0.00 -> 98.7 mm
- net GND: track 0.00 -> 36.8 mm
- net /R10_R8: track 0.00 -> 28.9 mm, vias 0 -> 1
- net /R10_R7: track 0.00 -> 24.1 mm, vias 0 -> 1
- net /7seg_CC6: track 0.00 -> 22.2 mm, vias 0 -> 1
- net /R10_R6: track 0.00 -> 19.6 mm, vias 0 -> 1
- net /R10_R1: track 0.00 -> 18.1 mm, vias 0 -> 1
- net /7seg_CC4: track 0.00 -> 16.8 mm, vias 0 -> 1
- net /7seg_CC5: track 0.00 -> 16.2 mm, vias 0 -> 1
- net /SR_MOSI: track 1.34 -> 17.5 mm
- net /R5_AIN: track 0.00 -> 15.4 mm
- net /R10_AIN: track 0.00 -> 14.7 mm
- net /G6R6_AIN: track 0.00 -> 13.3 mm
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- added copper zone on In2.Cu, net +5VD
